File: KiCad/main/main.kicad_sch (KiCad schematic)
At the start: 29 parts, among them J1 Hexpansion-Connector, U1 TCA8418, U4 ZD24C64A-XGMT

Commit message: Revert "Test App for PWM LED control"
This reverts commit 16f5d63235216fa5ad93ad454a595f19e9ea91df.
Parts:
- added C1: 10uF, Capacitor_SMD:C_0603_1608Metric_Pad1.08x0.95mm_HandSolder, symbol Device:C
- added C2: 1uF, Capacitor_SMD:C_0603_1608Metric_Pad1.08x0.95mm_HandSolder, symbol Device:C
- added D1: LED, LED_SMD:LED_0603_1608Metric_Pad1.05x0.95mm_HandSolder, symbol Device:LED
- added D10: 1N5819WS, Diode_SMD:D_SOD-323, symbol Diode:1N5819WS
- added L1: 6.8uH, Inductor_SMD:L_0603_1608Metric_Pad1.05x0.95mm_HandSolder, symbol Device:L
- added R1: 3k3, Resistor_SMD:R_0603_1608Metric_Pad0.98x0.95mm_HandSolder, symbol Device:R
- added R4: 20R, Resistor_SMD:R_0603_1608Metric_Pad0.98x0.95mm_HandSolder, symbol Device:R
- added R5: 100k, Resistor_SMD:R_0603_1608Metric_Pad0.98x0.95mm_HandSolder, symbol Device:R
- added U2: AP3032AKTR, Package_TO_SOT_SMD:SOT-23-6, symbol Driver_LED:AP3019AKTR
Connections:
- net !INT: now also J1.2 (LS_A); no longer J1.12 (HS_F)
- net GND: now also C1.2, C2.2, D1.1 (K), R4.2, R5.2, U2.2 (GND)
- net RST: now also J1.3 (LS_B); no longer J1.13 (HS_G)
- net VCC: now also C1.1, L1.1, R1.2, U2.6 (V_{IN}); no longer D2.2 (A), D3.2 (A), D4.2 (A), D5.2 (A), D6.2 (A), D7.2 (A), D8.2 (A), D9.2 (A)
- new net: D1.2 (A), R1.1
- new net: D2.1 (K), D6.1 (K), R4.1, U2.3 (FB)
- new net: D6.2 (A), D7.1 (K)
- new net: D10.2 (A), L1.2, U2.1 (SW)
- new net: D4.2 (A), D5.1 (K)
- new net: D3.2 (A), D4.1 (K)
- new net: D8.2 (A), D9.1 (K)
- new net: D7.2 (A), D8.1 (K)
- new net: D2.2 (A), D3.1 (K)
- new net LED_CTRL: J1.7 (LS_C), R5.1, U2.4 (CTRL)
- new net VDD: C2.1, D10.1 (K), D5.2 (A), D9.2 (A), U2.5 (V_{OUT})
- now unconnected: J1.8 (LS_D)
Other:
- moved on the sheet: D2, D3, D4, D5, D6, D7, D8, D9

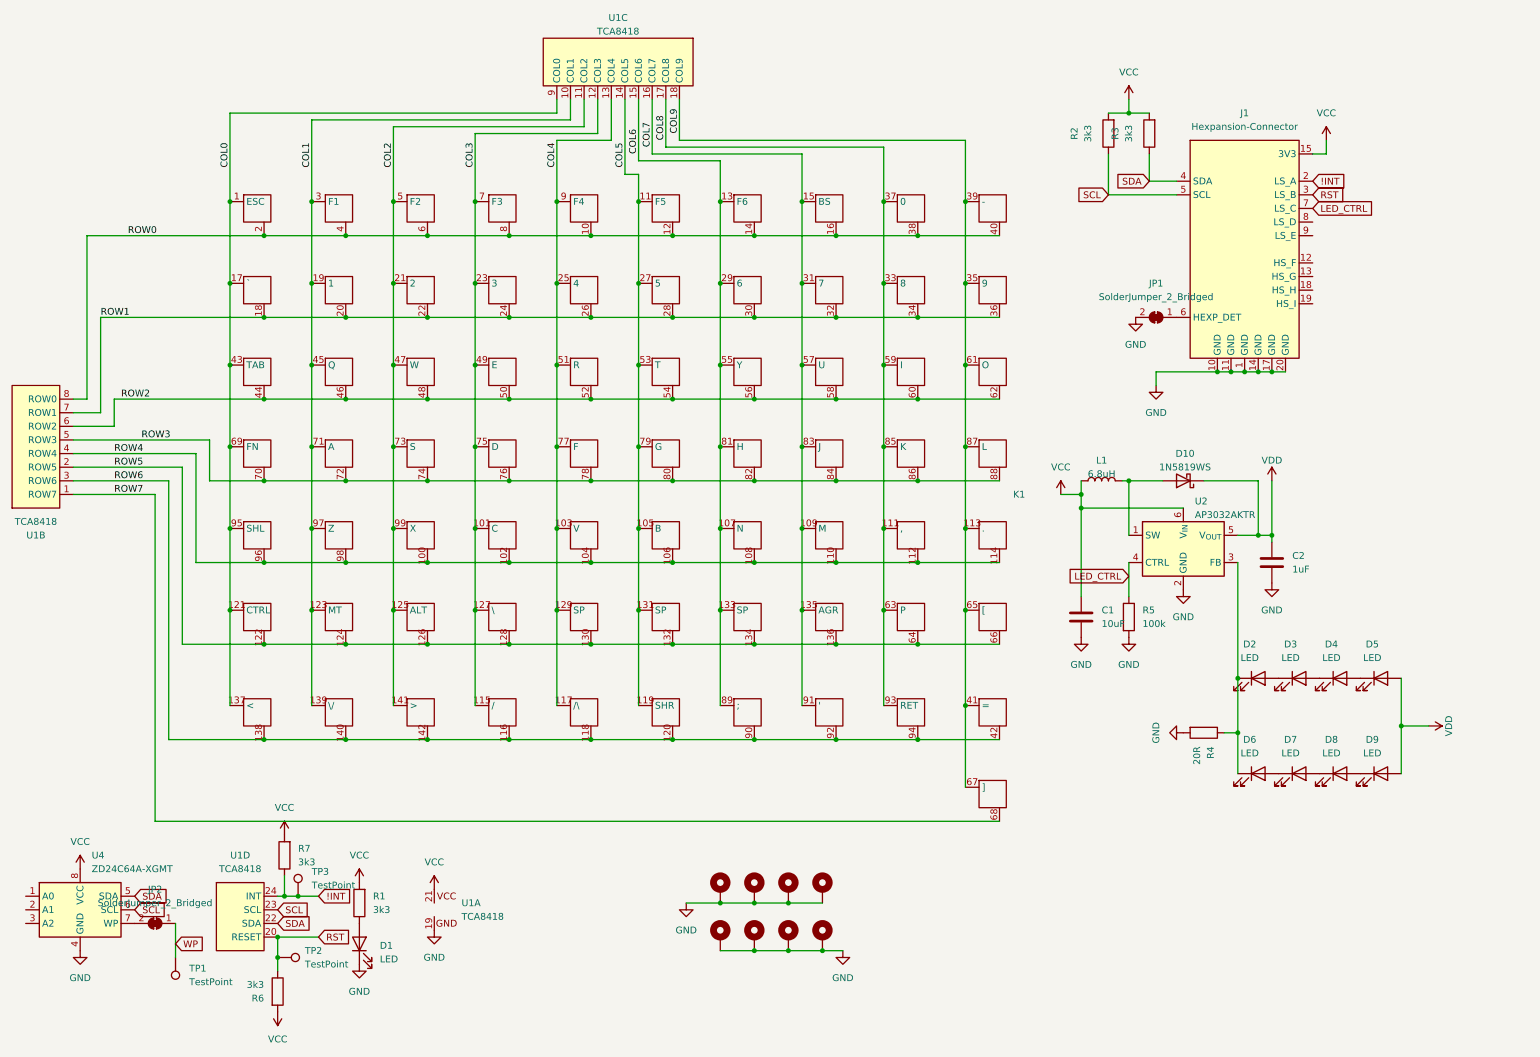
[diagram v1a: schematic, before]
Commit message: Test App for PWM LED control
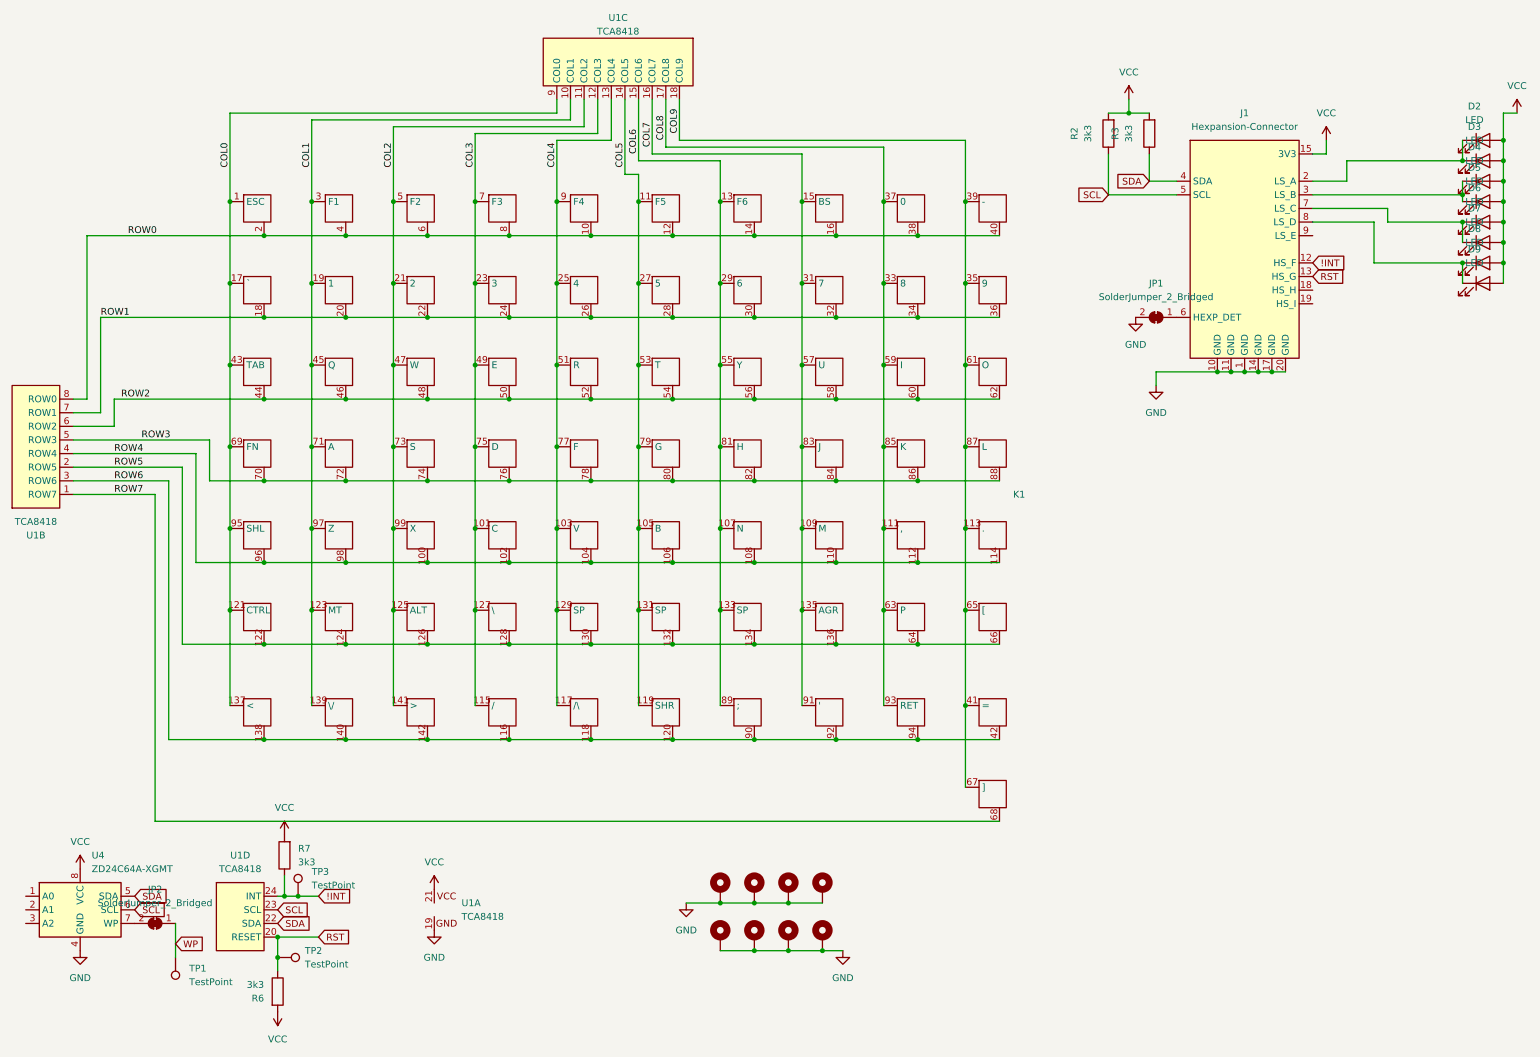
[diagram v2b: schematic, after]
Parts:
- removed C1: 10uF, Capacitor_SMD:C_0603_1608Metric_Pad1.08x0.95mm_HandSolder, symbol Device:C
- removed C2: 1uF, Capacitor_SMD:C_0603_1608Metric_Pad1.08x0.95mm_HandSolder, symbol Device:C
- removed D1: LED, LED_SMD:LED_0603_1608Metric_Pad1.05x0.95mm_HandSolder, symbol Device:LED
- removed D10: 1N5819WS, Diode_SMD:D_SOD-323, symbol Diode:1N5819WS
- removed L1: 6.8uH, Inductor_SMD:L_0603_1608Metric_Pad1.05x0.95mm_HandSolder, symbol Device:L
- removed R1: 3k3, Resistor_SMD:R_0603_1608Metric_Pad0.98x0.95mm_HandSolder, symbol Device:R
- removed R4: 20R, Resistor_SMD:R_0603_1608Metric_Pad0.98x0.95mm_HandSolder, symbol Device:R
- removed R5: 100k, Resistor_SMD:R_0603_1608Metric_Pad0.98x0.95mm_HandSolder, symbol Device:R
- removed U2: AP3032AKTR, Package_TO_SOT_SMD:SOT-23-6, symbol Driver_LED:AP3019AKTR
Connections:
- net LED_CTRL is gone; now on an unnamed net: J1.7 (LS_C)
- net VDD is gone; now on net VCC: D5.2 (A), D9.2 (A)
- net !INT: now also J1.12 (HS_F); no longer J1.2 (LS_A)
- net RST: now also J1.13 (HS_G); no longer J1.3 (LS_B)
- net VCC: now also D2.2 (A), D3.2 (A), D4.2 (A), D6.2 (A), D7.2 (A), D8.2 (A)
- net at D6.1 (K): now also D7.1 (K); no longer D2.1 (K)
- net at D5.1 (K): now also D4.1 (K), J1.3 (LS_B); no longer D4.2 (A)
- net at D9.1 (K): now also D8.1 (K), J1.8 (LS_D); no longer D8.2 (A)
- net at D3.1 (K): now also D2.1 (K), J1.2 (LS_A); no longer D2.2 (A)
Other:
- moved on the sheet: D2, D3, D4, D5, D6, D7, D8, D9
